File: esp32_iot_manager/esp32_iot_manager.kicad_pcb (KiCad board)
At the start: 4 copper layers, 81 x 55.2 mm, 89 parts, among them J1 SS-52400-002, J2 B2B-PH-SM4-TB, J3 GSD090012SEU, J4 Conn_01x04_Pin, J5 Conn_01x05_Pin, Q1 TEMT6000X01, Q2 BC817, Q3 BC817, U1 MCP73871, U2 BME280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

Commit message: FIX DRC
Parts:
- added TP7: 5V, TestPoint:TestPoint_Pad_D1.0mm, F.Cu at (157.5, 106.6)
- TP2: value MISO -> MISO
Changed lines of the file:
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@@
 			)
 		)
-		(property "Value" "MISO"
+		(property "Value" " MISO"
 			(at 0.03 -1.4 180)
 			(layer "F.SilkS")
@@
 		)
 	)
+	(footprint "TestPoint:TestPoint_Pad_D1.0mm"
+		(layer "F.Cu")
+		(at 157.47 106.63)
+		(descr "SMD pad as test Point, diameter 1.0mm")
+		(tags "test point SMD pad")
+		(property "Reference" "TP7"
+			(at 0 -1.448 0)
+			(layer "F.SilkS")
+			(hide yes)
+			(effects
+				(font
+					(size 1 1)
+					(thickness 0.15)
+				)
+			)
+		)
+		(property "Value" "5V"
+			(at 0 -1.35 0)
+			(layer "F.SilkS")
+			(effects
+				(font
+					(size 0.5 0.5)
+					(thickness 0.1)
+				)
+			)
+		)
+		(property "Datasheet" "~"
+			(at 0 0 0)
+			(unlocked yes)
+			(layer "F.Fab")
+			(hide yes)
+			(effects
+				(font
+					(size 1.27 1.27)
+					(thickness 0.15)
+				)
+			)
+		)
+		(property "Description" "test point"
+			(at 0 0 0)
+			(unlocked yes)
+			(layer "F.Fab")
+			(hide yes)
+			(effects
+				(font
+					(size 1.27 1.27)
+					(thickness 0.15)
+				)
+			)
+		)
+		(property ki_fp_filters "Pin* Test*")
+		(sheetname "/ESP32-C3-02/")
+		(sheetfile "ESP32-C3-02.kicad_sch")
+		(attr exclude_from_pos_files)
+		(fp_circle
+			(center 0 0)
+			(end 0 0.7)
+			(stroke
+				(width 0.12)
+				(type solid)
+			)
+			(fill no)
+			(layer "F.SilkS")
+		)
+		(fp_circle
+			(center 0 0)
+			(end 1 0)
+			(stroke
+				(width 0.05)
+				(type solid)
+			)
+			(fill no)
+			(layer "F.CrtYd")
+		)
+		(fp_text user "${REFERENCE}"
+			(at 0 -1.45 0)
+			(layer "F.Fab")
+			(effects
+				(font
+					(size 1 1)
+					(thickness 0.15)
+				)
+			)
+		)
+		(pad "1" smd circle
+			(at 0 0)
+			(size 1 1)
+			(layers "F.Cu" "F.Mask")
+			(net 3 "+5V")
+			(pinfunction "1")
+			(pintype "passive")
+		)
+		(embedded_fonts no)
+	)
 	(footprint "esp32_manager_project:MODULE_ESP32-C3-WROOM-02-H4"

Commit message: 3d models
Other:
- board text added: "BOOT"
- board text added: "RESET"
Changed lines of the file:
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@@
 	(net 77 "Net-(C22-Pad2)")
 	(footprint "esp32_manager_project:SW_USLPT2819DT2TR"
-		(locked yes)
 		(layer "F.Cu")
 		(at 179.35 112.4)
@@
 			(at 0.025 1.58 0)
 			(layer "F.Fab")
+			(hide yes)
 			(effects
 				(font
@@
 		)
 		(embedded_fonts no)
-		(model "LTST-C170KRKT.stp"
+		(model "${ESP32_IOT_MANAGER_3D_MODELS}/LTST-C170KRKT.stp"
 			(offset
 				(xyz -0.7699999694 -0.6199999955 0.3499999888)
@@
 	)
 	(footprint "Package_TO_SOT_SMD:SOT-23"
-		(locked yes)
 		(layer "F.Cu")
 		(at 185.6 103.2125 90)
@@
 	)
 	(footprint "Resistor_SMD:R_0805_2012Metric"
-		(locked yes)
 		(layer "F.Cu")
 		(at 185.4984 106.3875)
@@
 		)
 		(embedded_fonts no)
-		(model "T491A106K010AT7280.stp"
+		(model "${ESP32_IOT_MANAGER_3D_MODELS}/T491A106K010AT7280.stp"
 			(offset
 				(xyz -1.570000029 -0.8999999626 0)
@@
 	)
 	(footprint "Resistor_SMD:R_0805_2012Metric"
-		(locked yes)
 		(layer "F.Cu")
 		(at 179.3678 106.4503)
@@
 	)
 	(footprint "Capacitor_SMD:C_0805_2012Metric"
-		(locked yes)
 		(layer "F.Cu")
 		(at 185.4298 109.1919 180)
@@
 		)
 		(embedded_fonts no)
-		(model "LTST-C170KRKT.stp"
+		(model "${ESP32_IOT_MANAGER_3D_MODELS}/LTST-C170KRKT.stp"
 			(offset
 				(xyz -0.7699999694 -0.6199999955 0.3499999888)
@@
 		)
 		(embedded_fonts no)
-		(model "LTST-C170KRKT.stp"
+		(model "${ESP32_IOT_MANAGER_3D_MODELS}/LTST-C170KRKT.stp"
 			(offset
 				(xyz -0.7699999694 -0.6199999955 0.3499999888)
@@
 		)
 		(embedded_fonts no)
-		(model "T491A106K010AT7280.stp"
+		(model "${ESP32_IOT_MANAGER_3D_MODELS}/T491A106K010AT7280.stp"
 			(offset
 				(xyz -1.570000029 -0.8999999626 0)
@@
 		)
 		(embedded_fonts no)
-		(model "LTST-C170KRKT.stp"
+		(model "${ESP32_IOT_MANAGER_3D_MODELS}/LTST-C170KRKT.stp"
 			(offset
 				(xyz -0.7699999694 -0.6199999955 0.3499999888)
@@
 		)
 		(embedded_fonts no)
-		(model "0ZCH0110AF2E.stp"
+		(model "${ESP32_IOT_MANAGER_3D_MODELS}/0ZCH0110AF2E.stp"
 			(offset
 				(xyz 0 0 0.4)
@@
 		)
 		(embedded_fonts no)
-		(model "T491A106K010AT7280.stp"
+		(model "${ESP32_IOT_MANAGER_3D_MODELS}/T491A106K010AT7280.stp"
 			(offset
 				(xyz -1.570000029 -0.8999999626 0)
@@
 		)
 		(embedded_fonts no)
-		(model "LTST-C170KRKT.stp"
+		(model "${ESP32_IOT_MANAGER_3D_MODELS}/LTST-C170KRKT.stp"
 			(offset
 				(xyz -0.7699999694 -0.6199999955 0.3499999888)
@@
 		)
 		(embedded_fonts no)
-		(model "T491A106K010AT7280.stp"
+		(model "${ESP32_IOT_MANAGER_3D_MODELS}/T491A106K010AT7280.stp"
 			(offset
 				(xyz -1.570000029 -0.8999999626 0)
@@
 	)
 	(footprint "Resistor_SMD:R_0805_2012Metric"
-		(locked yes)
 		(layer "F.Cu")
 		(at 175.9134 111.909 90)
@@
 	)
 	(footprint "Package_TO_SOT_SMD:SOT-23"
-		(locked yes)
 		(layer "F.Cu")
 		(at 179.3678 103.3238 90)
@@
 	)
 	(footprint "Capacitor_SMD:C_0805_2012Metric"
-		(locked yes)
 		(layer "F.Cu")
 		(at 179.2764 109.2547)
@@
 		)
 		(embedded_fonts no)
-		(model "T491A106K010AT7280.stp"
+		(model "${ESP32_IOT_MANAGER_3D_MODELS}/T491A106K010AT7280.stp"
 			(offset
 				(xyz -1.570000029 -0.8999999626 0)
@@
 	)
 	(footprint "esp32_manager_project:SW_USLPT2819DT2TR"
-		(locked yes)
 		(layer "F.Cu")
 		(at 185.4324 112.3672)
@@
 			(at 0 1.6936 0)
 			(layer "F.Fab")
+			(hide yes)
 			(effects
 				(font
@@
 		)
 		(embedded_fonts no)
-		(model "LTST-C170KRKT.stp"
+		(model "${ESP32_IOT_MANAGER_3D_MODELS}/LTST-C170KRKT.stp"
 			(offset
 				(xyz -0.7699999694 -0.6199999955 0.3499999888)
@@
 		(layer "Edge.Cuts")
 	)
+	(gr_text "RESET"
+		(at 178.25 114.5 0)
+		(layer "F.SilkS")
+		(effects
+			(font
+				(size 0.5 0.5)
+				(thickness 0.125)
+				(bold yes)
+			)
+			(justify left bottom)
+		)
+	)
+	(gr_text "BOOT"
+		(at 184.5 114.5 0)
+		(layer "F.SilkS")
+		(effects
+			(font
+				(size 0.5 0.5)
+				(thickness 0.125)
+				(bold yes)
+			)
+			(justify left bottom)
+		)
+	)
 	(segment

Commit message: production build for manufacturing
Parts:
- removed the REF** at (141.8, 91.9)
- added G***: LOGO, JPI_LOGOS:jpi_logo_text_10mm_silkscreen, B.Cu at (212.2, 110.8)
- added G***: LOGO, JPI_LOGOS:jpi_logo_10mm_silkscreen, B.Cu at (141.8, 110.8)
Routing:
- net GND: track 149.5 -> 143.8 mm
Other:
- board size 81 x 55.2 mm -> 81.7 x 55.2 mm
- board text added: "3.3V"
- board text added: "CHARGED"
- board text added: "CHARGING"
- board text added: "ESP32 IOT Manager V1 Designed by: Jose Padilla"
- board text added: "GND"
- board text added: "GPIO18"
- board text added: "GPIO19"
- board text added: "GPIO8"
- board text added: "POWER OK"
- board text added: "SCL"
- board text added: "SDA"

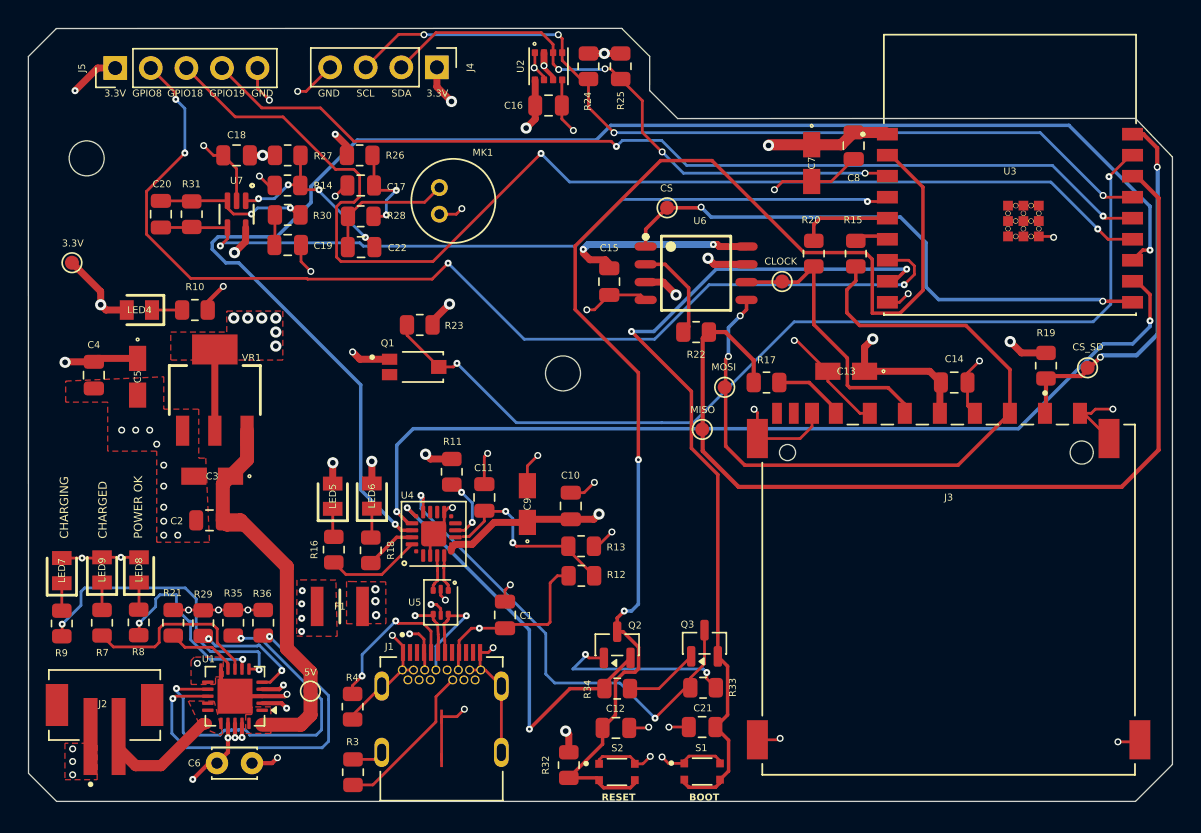
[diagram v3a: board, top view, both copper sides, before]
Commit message: flip transistor
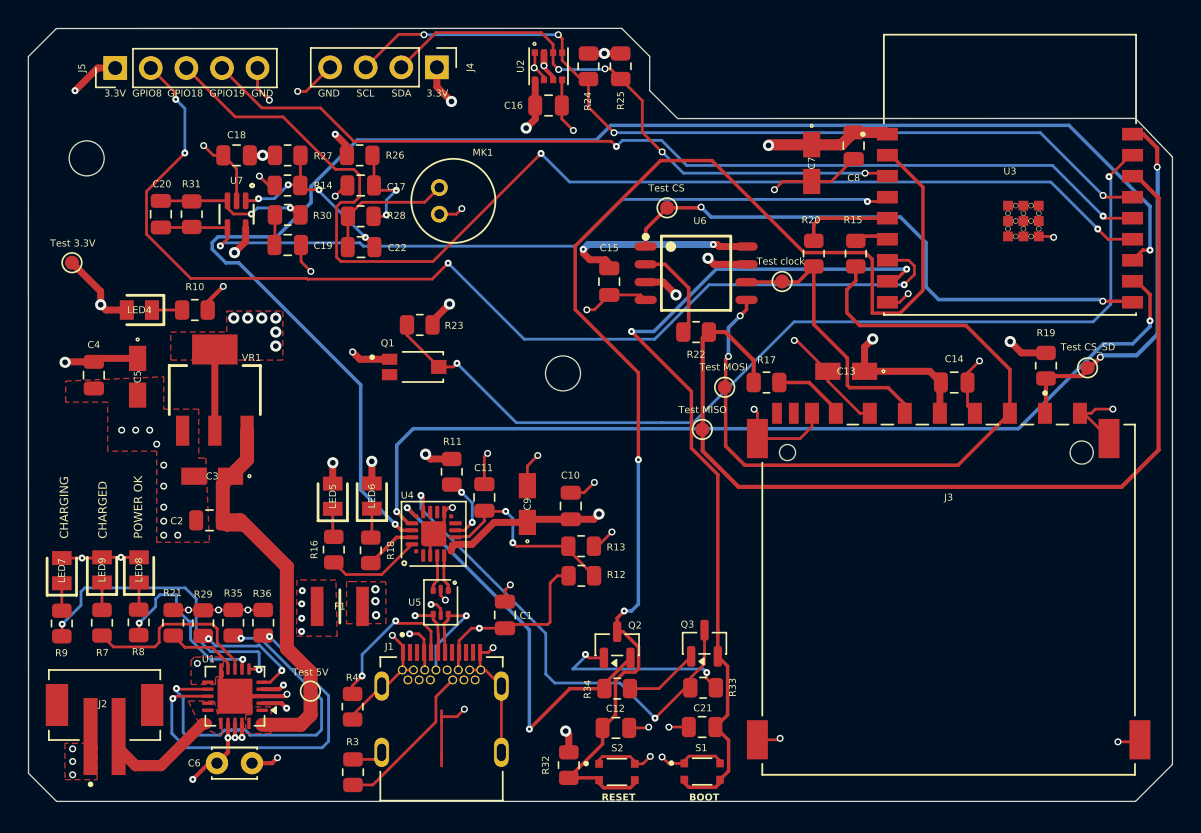
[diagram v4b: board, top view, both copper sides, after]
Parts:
- TP1: value MOSI -> Test MOSI
- TP2: value MISO -> Test MISO
- TP3: value CLOCK -> Test clock
- TP4: value CS -> Test CS
- TP5: value CS_SD -> Test CS_SD
- TP6: value 3.3V -> Test 3.3V
- TP7: value 5V -> Test 5V
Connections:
- Q3 pad 2: /ESP32-C3-02/BOOT -> /ESP32-C3-02/DTR
- Q3 pad 3: /ESP32-C3-02/DTR -> /ESP32-C3-02/BOOT
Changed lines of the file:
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@@
 			)
 		)
-		(property "Value" "CS_SD"
+		(property "Value" "Test CS_SD"
 			(at 0.03 -1.48 0)
 			(layer "F.SilkS")
@@
 			(layers "F.Cu" "F.Mask" "F.Paste")
 			(roundrect_rratio 0.25)
-			(net 11 "/ESP32-C3-02/BOOT")
+			(net 26 "/ESP32-C3-02/DTR")
 			(pinfunction "E")
 			(pintype "passive")
@@
 			(layers "F.Cu" "F.Mask" "F.Paste")
 			(roundrect_rratio 0.25)
-			(net 26 "/ESP32-C3-02/DTR")
+			(net 11 "/ESP32-C3-02/BOOT")
 			(pinfunction "C")
 			(pintype "passive")
@@
 			)
 		)
-		(property "Value" "MOSI"
+		(property "Value" "Test MOSI"
 			(at -0.07 -1.44 0)
 			(layer "F.SilkS")
@@
 			)
 		)
-		(property "Value" " MISO"
+		(property "Value" "Test MISO"
 			(at 0.03 -1.4 180)
 			(layer "F.SilkS")
@@
 			)
 		)
-		(property "Value" "CS"
+		(property "Value" "Test CS"
 			(at -0.04 -1.4 0)
 			(layer "F.SilkS")
@@
 			)
 		)
-		(property "Value" "CLOCK"
+		(property "Value" "Test clock"
 			(at -0.1 -1.44 0)
 			(layer "F.SilkS")
@@
 			)
 		)
-		(property "Value" "5V"
+		(property "Value" "Test 5V"
 			(at 0 -1.35 0)
 			(layer "F.SilkS")
@@
 			)
 		)
-		(property "Value" "3.3V"
+		(property "Value" "Test 3.3V"
 			(at 0.06 -1.39 0)
 			(layer "F.SilkS")
